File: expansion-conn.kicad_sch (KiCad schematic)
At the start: 3 parts, among them J1 J_ERM8-040-XX.X-X-DV-XX_SAMTEC

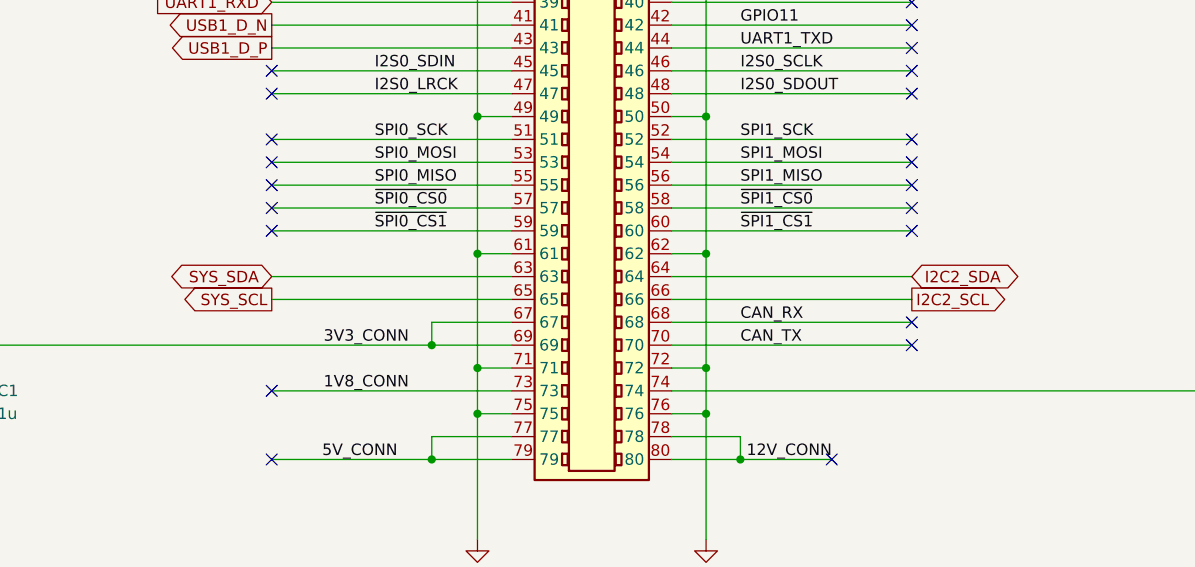
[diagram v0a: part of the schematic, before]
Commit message: [#45990] Fix schematic flaws discussed in review
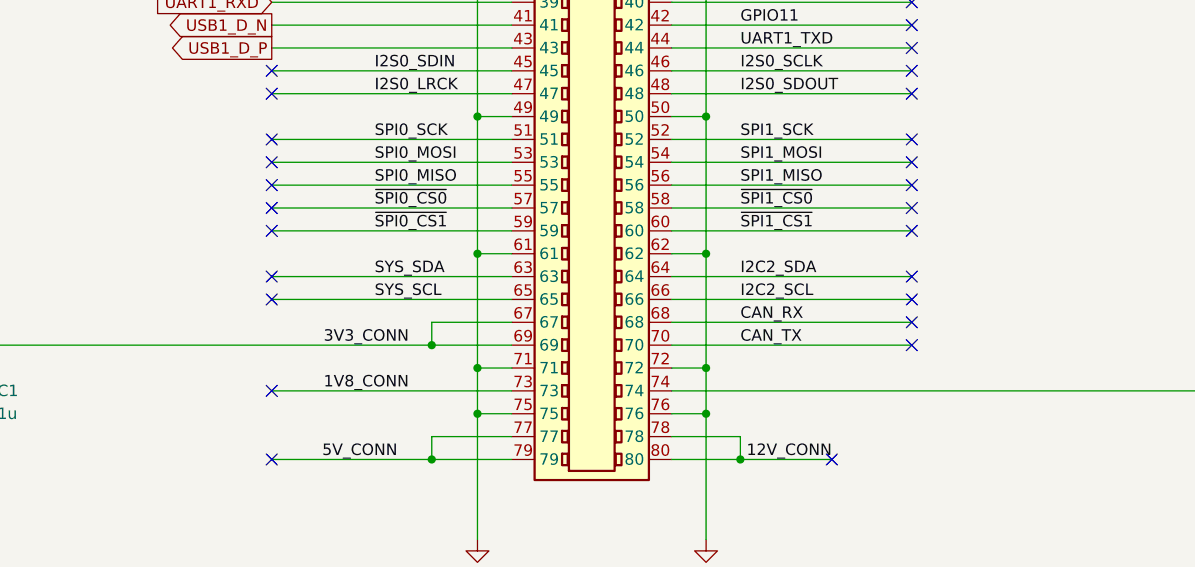
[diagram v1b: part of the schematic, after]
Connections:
- no-connect marks 35 -> 39
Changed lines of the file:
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@@
   (no_connect (at 173.99 100.33))
   (no_connect (at 173.99 146.05))
+  (no_connect (at 173.99 153.67))
   (no_connect (at 245.11 158.75))
+  (no_connect (at 245.11 156.21))
   (no_connect (at 173.99 130.81))
   (no_connect (at 173.99 133.35))
@@
   (no_connect (at 245.11 146.05))
   (no_connect (at 245.11 95.25))
+  (no_connect (at 173.99 156.21))
   (no_connect (at 245.11 133.35))
   (no_connect (at 245.11 143.51))
+  (no_connect (at 245.11 153.67))
   (no_connect (at 173.99 148.59))
   (no_connect (at 173.99 173.99))
@@
     (effects (font (size 1.27 1.27)) (justify left bottom))
   )
+  (label "SYS_SDA" (at 185.42 153.67 0)
+    (effects (font (size 1.27 1.27)) (justify left bottom))
+  )
   (label "SPI1_MISO" (at 226.06 143.51 0)
+    (effects (font (size 1.27 1.27)) (justify left bottom))
+  )
+  (label "I2C2_SDA" (at 226.06 153.67 0)
     (effects (font (size 1.27 1.27)) (justify left bottom))
   )
@@
     (effects (font (size 1.27 1.27)) (justify left bottom))
   )
+  (label "SYS_SCL" (at 185.42 156.21 0)
+    (effects (font (size 1.27 1.27)) (justify left bottom))
+  )
   (label "USBSS1_RX_P" (at 226.06 105.41 0)
     (effects (font (size 1.27 1.27)) (justify left bottom))
@@
   )
   (label "GPIO07" (at 186.69 115.57 0)
+    (effects (font (size 1.27 1.27)) (justify left bottom))
+  )
+  (label "I2C2_SCL" (at 226.06 156.21 0)
     (effects (font (size 1.27 1.27)) (justify left bottom))
   )
@@
     )
   )
-  (global_label "I2C2_SDA" (shape bidirectional) (at 245.11 153.67 0) (fields_autoplaced)
-    (effects (font (size 1.27 1.27)) (justify left))
-    (property "Intersheet References" "${INTERSHEET_REFS}" (id 0) (at 256.3526 153.5906 0)
-      (effects (font (size 1.27 1.27)) (justify left))
-    )
-  )
-  (global_label "SYS_SDA" (shape bidirectional) (at 173.99 153.67 180) (fields_autoplaced)
-    (effects (font (size 1.27 1.27)) (justify right))
-    (property "Intersheet References" "${INTERSHEET_REFS}" (id 0) (at 163.5336 153.5906 0)
-      (effects (font (size 1.27 1.27)) (justify right))
-    )
-  )
   (global_label "PCIE2_CLK_P" (shape output) (at 173.99 95.25 180) (fields_autoplaced)
     (effects (font (size 1.27 1.27)) (justify right))
@@
     )
   )
-  (global_label "SYS_SCL" (shape output) (at 173.99 156.21 180) (fields_autoplaced)
-    (effects (font (size 1.27 1.27)) (justify right))
-    (property "Intersheet References" "${INTERSHEET_REFS}" (id 0) (at 163.594 156.1306 0)
-      (effects (font (size 1.27 1.27)) (justify right))
-    )
-  )
   (global_label "PCIE2_RX0_N" (shape input) (at 245.11 87.63 0) (fields_autoplaced)
     (effects (font (size 1.27 1.27)) (justify left))
@@
       (effects (font (size 1.27 1.27)) (justify left))
     )
-  )
-  (global_label "I2C2_SCL" (shape output) (at 245.11 156.21 0) (fields_autoplaced)
-    (effects (font (size 1.27 1.27)) (justify left))
-    (property "Intersheet References" "${INTERSHEET_REFS}" (id 0) (at 256.2921 156.1306 0)
-      (effects (font (size 1.27 1.27)) (justify left))
-    )

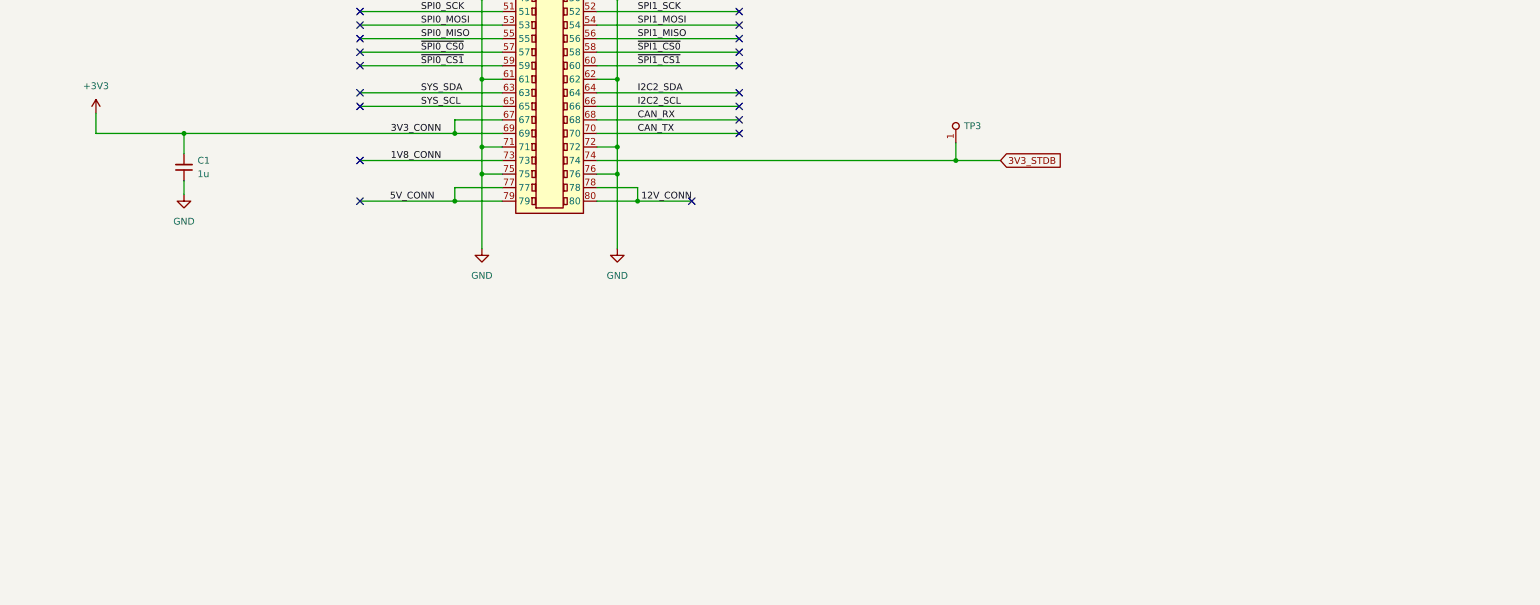
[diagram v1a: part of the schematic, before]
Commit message: [#45990] Route dif Pcie, place susclk gen
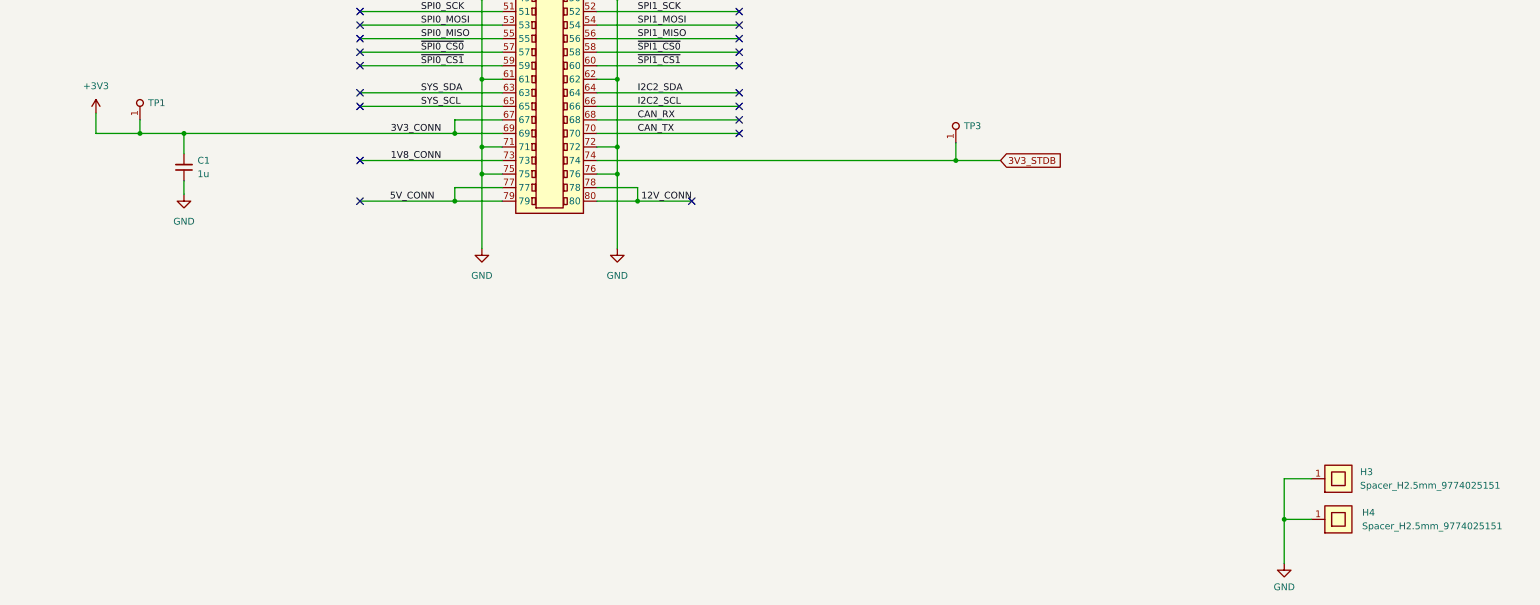
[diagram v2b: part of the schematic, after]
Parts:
- added H3, H4: Spacer_H2.5mm_9774025151, antmicro-footprints:Spacer_SMD_M2.5_H2.5mm_Wurth_9774025151, symbol antmicroMechanicalParts:Spacer_H2.5mm_9774025151
- added TP1: TP_0.75mm_SMD, antmicro-footprints:TP_SMD_0.75mm, symbol antmicroTestPoints:TP_0.75mm_SMD
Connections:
- net +3V3: now also TP1.1
- net GND: now also H3.1, H4.1
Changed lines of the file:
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@@
     (company "Antmicro Ltd")
   )
+  (junction (at 132.715 161.29) (diameter 0) (color 0 0 0 0)
+  )
   (junction (at 196.85 82.55) (diameter 0) (color 0 0 0 0)
   )
@@
   )
   (junction (at 140.97 161.29) (diameter 0) (color 0 0 0 0)
+  )
+  (junction (at 347.345 233.68) (diameter 0) (color 0 0 0 0)
   )
   (junction (at 285.75 166.37) (diameter 0) (color 0 0 0 0)
@@
     (stroke (width 0) (type default) (color 0 0 0 0))
   )
+  (wire (pts (xy 132.715 158.75) (xy 132.715 161.29))
+    (stroke (width 0) (type default) (color 0 0 0 0))
+  )
   (wire (pts (xy 245.11 87.63) (xy 218.44 87.63))
     (stroke (width 0) (type default) (color 0 0 0 0))
@@
     (stroke (width 0) (type default) (color 0 0 0 0))
   )
-  (wire (pts (xy 124.46 161.29) (xy 140.97 161.29))
+  (wire (pts (xy 124.46 161.29) (xy 132.715 161.29))
     (stroke (width 0) (type default) (color 0 0 0 0))
   )
@@
     (stroke (width 0) (type default) (color 0 0 0 0))
   )
+  (wire (pts (xy 347.345 226.06) (xy 347.345 233.68))
+    (stroke (width 0) (type default) (color 0 0 0 0))
+  )
   (wire (pts (xy 245.11 95.25) (xy 218.44 95.25))
     (stroke (width 0) (type default) (color 0 0 0 0))
@@
     (stroke (width 0) (type default) (color 0 0 0 0))
   )
+  (wire (pts (xy 352.425 226.06) (xy 347.345 226.06))
+    (stroke (width 0) (type default) (color 0 0 0 0))
+  )
   (wire (pts (xy 173.99 118.11) (xy 200.66 118.11))
     (stroke (width 0) (type default) (color 0 0 0 0))
@@
     (stroke (width 0) (type default) (color 0 0 0 0))
   )
+  (wire (pts (xy 347.345 233.68) (xy 352.425 233.68))
+    (stroke (width 0) (type default) (color 0 0 0 0))
+  )
   (wire (pts (xy 222.25 74.93) (xy 218.44 74.93))
     (stroke (width 0) (type default) (color 0 0 0 0))
@@
     (stroke (width 0) (type default) (color 0 0 0 0))
   )
+  (wire (pts (xy 347.345 233.68) (xy 347.345 241.935))
+    (stroke (width 0) (type default) (color 0 0 0 0))
+  )
   (wire (pts (xy 245.11 90.17) (xy 218.44 90.17))
     (stroke (width 0) (type default) (color 0 0 0 0))
@@
   )
   (wire (pts (xy 226.06 173.99) (xy 236.22 173.99))
+    (stroke (width 0) (type default) (color 0 0 0 0))
+  )
+  (wire (pts (xy 132.715 161.29) (xy 140.97 161.29))
     (stroke (width 0) (type default) (color 0 0 0 0))
   )
@@
     )
   )
+  (symbol (lib_id "antmicropower:GND") (at 347.345 241.935 0) (unit 1)
+    (in_bom yes) (on_board yes) (fields_autoplaced)
+    (property "Reference" "#PWR0118" (id 0) (at 347.345 248.285 0)
+      (effects (font (size 1.27 1.27)) hide)
+    )
+    (property "Value" "GND" (id 1) (at 347.345 246.38 0))
+    (property "Footprint" "" (id 2) (at 347.345 241.935 0)
+      (effects (font (size 1.27 1.27)) hide)
+    )
+    (property "Datasheet" "" (id 3) (at 347.345 241.935 0)
+      (effects (font (size 1.27 1.27)) hide)
+    )
+    (pin "1")
+  )
+  (symbol (lib_id "antmicroMechanicalParts:Spacer_H2.5mm_9774025151") (at 352.425 233.68 0) (unit 1)
+    (in_bom yes) (on_board yes) (fields_autoplaced)
+    (property "Reference" "H4" (id 0) (at 361.95 232.4099 0)
+      (effects (font (size 1.27 1.27) (thickness 0.15)) (justify left))
+    )
+    (property "Value" "Spacer_H2.5mm_9774025151" (id 1) (at 361.95 234.9499 0)
+      (effects (font (size 1.27 1.27) (thickness 0.15)) (justify left))
+    )
+    (property "Footprint" "antmicro-footprints:Spacer_SMD_M2.5_H2.5mm_Wurth_9774025151" (id 2) (at 375.285 241.3 0)
+      (effects (font (size 1.27 1.27) (thickness 0.15)) (justify left bottom) hide)
+    )
+    (property "Datasheet" "https://www.we-online.com/components/products/datasheet/9774025151.pdf" (id 3) (at 375.285 243.84 0)
+      (effects (font (size 1.27 1.27) (thickness 0.15)) (justify left bottom) hide)
+    )
+    (property "Manufacturer" "Würth Elektronik" (id 4) (at 375.285 246.38 0)
+      (effects (font (size 1.27 1.27) (thickness 0.15)) (justify left bottom) hide)
+    )
+    (property "MPN" "9774025151" (id 5) (at 375.285 248.92 0)
+      (effects (font (size 1.27 1.27) (thickness 0.15)) (justify left bottom) hide)
+    )
+    (property "Author" "Antmicro" (id 6) (at 375.285 251.46 0)
+      (effects (font (size 1.27 1.27) (thickness 0.15)) (justify left bottom) hide)
+    )
+    (property "License" "Apache-2.0" (id 7) (at 375.285 254 0)
+      (effects (font (size 1.27 1.27) (thickness 0.15)) (justify left bottom) hide)
+    )
+    (pin "1")
+  )
   (symbol (lib_id "antmicroCapacitors0402:C_1u_0402") (at 140.97 170.18 90) (unit 1)
     (in_bom yes) (on_board yes) (fields_autoplaced)
@@
     (pin "80")
   )
+  (symbol (lib_id "antmicroTestPoints:TP_0.75mm_SMD") (at 132.715 158.75 90) (unit 1)
+    (in_bom yes) (on_board yes) (fields_autoplaced)
+    (property "Reference" "TP1" (id 0) (at 134.239 155.5749 90)
+      (effects (font (size 1.27 1.27) (thickness 0.15)) (justify right))
+    )
+    (property "Value" "TP_0.75mm_SMD" (id 1) (at 140.335 143.51 0)
+      (effects (font (size 1.27 1.27) (thickness 0.15)) (justify left bottom) hide)
+    )
+    (property "Footprint" "antmicro-footprints:TP_SMD_0.75mm" (id 2) (at 142.875 143.51 0)
+      (effects (font (size 1.27 1.27) (thickness 0.15)) (justify left bottom) hide)
+    )
+    (property "Datasheet" "" (id 3) (at 145.415 143.51 0)
+      (effects (font (size 1.27 1.27) (thickness 0.15)) (justify left bottom) hide)
+    )
+    (property "MPN" "" (id 4) (at 132.715 158.75 0)
+      (effects (font (size 1.27 1.27)) hide)
+    )
+    (property "Manufacturer" "" (id 5) (at 132.715 158.75 0)
+      (effects (font (size 1.27 1.27)) hide)
+    )
+    (property "Author" "Antmicro" (id 6) (at 147.955 143.51 0)
+      (effects (font (size 1.27 1.27) (thickness 0.15)) (justify left bottom) hide)
+    )
+    (property "License" "Apache-2.0" (id 7) (at 150.495 143.51 0)
+      (effects (font (size 1.27 1.27) (thickness 0.15)) (justify left bottom) hide)
+    )
+    (pin "1")
+  )
   (symbol (lib_id "antmicropower:GND") (at 196.85 182.88 0) (unit 1)
     (in_bom yes) (on_board yes) (fields_autoplaced)
@@
       (effects (font (size 1.27 1.27) (thickness 0.15)) (justify left bottom) hide)
     )
+    (pin "1")
+  )
+  (symbol (lib_id "antmicroMechanicalParts:Spacer_H2.5mm_9774025151") (at 352.425 226.06 0) (unit 1)
+    (in_bom yes) (on_board yes) (fields_autoplaced)
+    (property "Reference" "H3" (id 0) (at 361.569 224.7899 0)
+      (effects (font (size 1.27 1.27) (thickness 0.15)) (justify left))
+    )
+    (property "Value" "Spacer_H2.5mm_9774025151" (id 1) (at 361.569 227.3299 0)
+      (effects (font (size 1.27 1.27) (thickness 0.15)) (justify left))
+    )
+    (property "Footprint" "antmicro-footprints:Spacer_SMD_M2.5_H2.5mm_Wurth_9774025151" (id 2) (at 375.285 233.68 0)
+      (effects (font (size 1.27 1.27) (thickness 0.15)) (justify left bottom) hide)
+    )
+    (property "Datasheet" "https://www.we-online.com/components/products/datasheet/9774025151.pdf" (id 3) (at 375.285 236.22 0)
+      (effects (font (size 1.27 1.27) (thickness 0.15)) (justify left bottom) hide)
+    )
+    (property "Manufacturer" "Würth Elektronik" (id 4) (at 375.285 238.76 0)
+      (effects (font (size 1.27 1.27) (thickness 0.15)) (justify left bottom) hide)
+    )
+    (property "MPN" "9774025151" (id 5) (at 375.285 241.3 0)
+      (effects (font (size 1.27 1.27) (thickness 0.15)) (justify left bottom) hide)
+    )
+    (property "Author" "Antmicro" (id 6) (at 375.285 243.84 0)
+      (effects (font (size 1.27 1.27) (thickness 0.15)) (justify left bottom) hide)
+    )
+    (property "License" "Apache-2.0" (id 7) (at 375.285 246.38 0)
+      (effects (font (size 1.27 1.27) (thickness 0.15)) (justify left bottom) hide)
+    )
